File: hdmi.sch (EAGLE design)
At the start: 130 parts, among them U0 6SLX45CSG324, U1 MT41J64M16, U2 TPD12S016RKTR, U3 TPD12S016RKTR, U4 TPD12S016RKTR, U5 MNR18, U6 MNR18

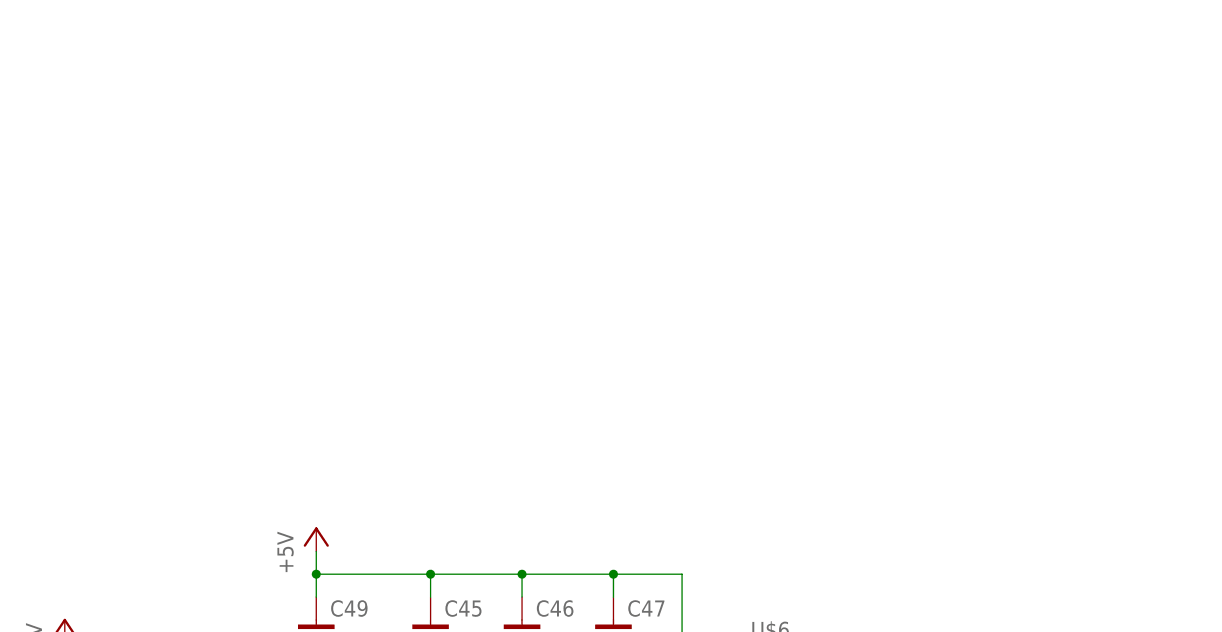
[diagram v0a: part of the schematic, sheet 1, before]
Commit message: +prj-hdmi.lbr, +5V protection
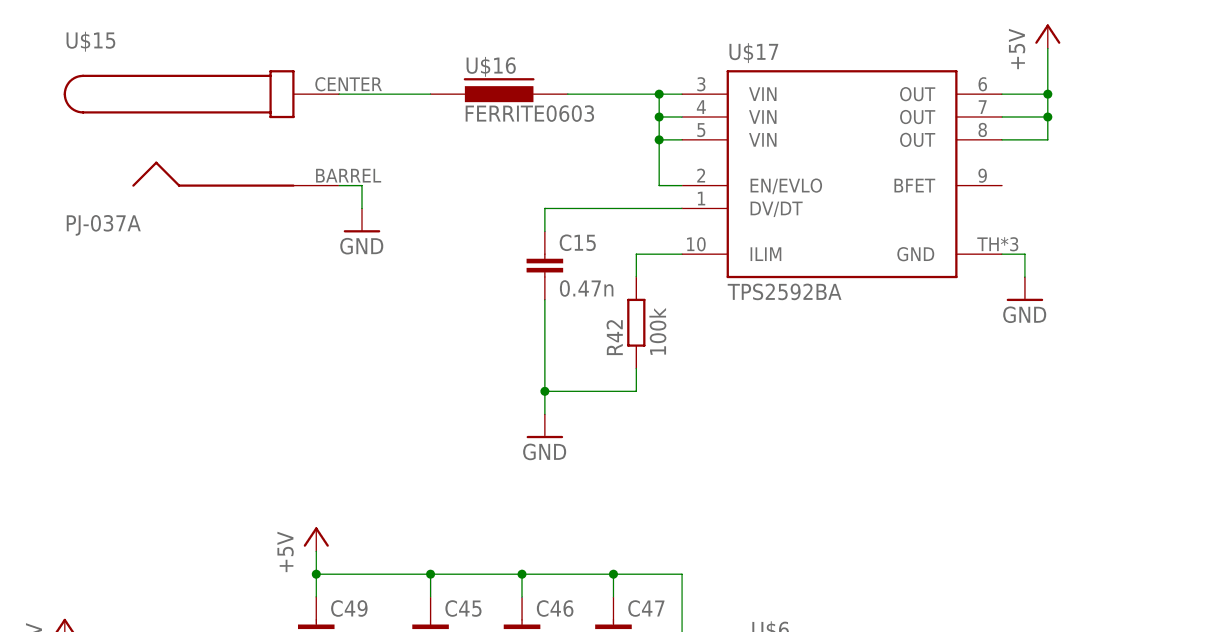
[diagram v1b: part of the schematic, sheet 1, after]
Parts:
- removed R43: 4.7k, resistor:R-EU_R0402
- removed U$12: PJ-037A, con-cui:PJ-037A
- removed U$13: FERRITE0603, inductors:FERRITE0603
- added C15: 0.47n, rcl:C-EUC0402
- added R46: 1k, resistor:R-EU_R0402
- added U$15: PJ-037A, prj-hdmi:PJ-037A
- added U$16: FERRITE0603, inductors:FERRITE0603
- added U$17: TPS2592BA, prj-hdmi:TPS2592BA
- CONN0, CONN1, CONN2: device con-fci:HDMI_TYPE_A_RECEPTICAL -> prj-hdmi:HDMI_TYPE_A_RECEPTICAL
- CONN3: device con-usb-3:USB-MB-S -> prj-hdmi:USB-MB-S
- IC1: device ftdichip-3:FT2232HQ -> prj-hdmi:FT2232HQ
- R42: value 10k -> 100k
- U$1: device Abracon:ABM8G -> prj-hdmi:ABM8G
- U$5: device Microchip_By_element14_Batch_1:93LC46BT-I/OT -> prj-hdmi:93LC46BT-I/OT
- U$6: device Micrel Inc:MIC23451AAAYFL -> prj-hdmi:MIC23451AAAYFL
- U$9: device memory-micron:N25Q128A13EF8 -> prj-hdmi:N25Q128A13EF8
- U0: device xilinx_devices_V6:6SLX45CSG324 -> prj-hdmi:6SLX45CSG324
- U1: device memory-micron:MT41J64M16 -> prj-hdmi:MT41J64M16
- U2, U3, U4: device Texas Instruments:TPD12S016RKTR -> prj-hdmi:TPD12S016RKTR
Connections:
- net N$49 renamed USB_5V_DISABLE
- removed net USB_5V_ERR: R45.1, U$10.ACK#
- new net N$32: C15.1, U$17.DV/DT
- new net N$36: R42.2, U$17.ILIM
- new net USB_5V_ACK#: R45.1, R46.1, U$10.ACK#
- new net USB_5V_OFF: R46.2
- net +3V3: now also R26.1
- net +5V: now also U$17.OUT@6, U$17.OUT@7, U$17.OUT@8; no longer R43.2
- net CENTER: now also U$15.CENTER, U$16.1; no longer U$12.CENTER, U$13.1
- net GND: now also C15.2, U$15.BARREL, U$17.GND; no longer U$12.BARREL
- net N$29: now also U$16.2, U$17.EN/EVLO, U$17.VIN@3, U$17.VIN@4, U$17.VIN@5; no longer R26.1
- net USB_PWRSAVE#: no longer R42.2, R43.1
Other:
- moved on the sheet: R45

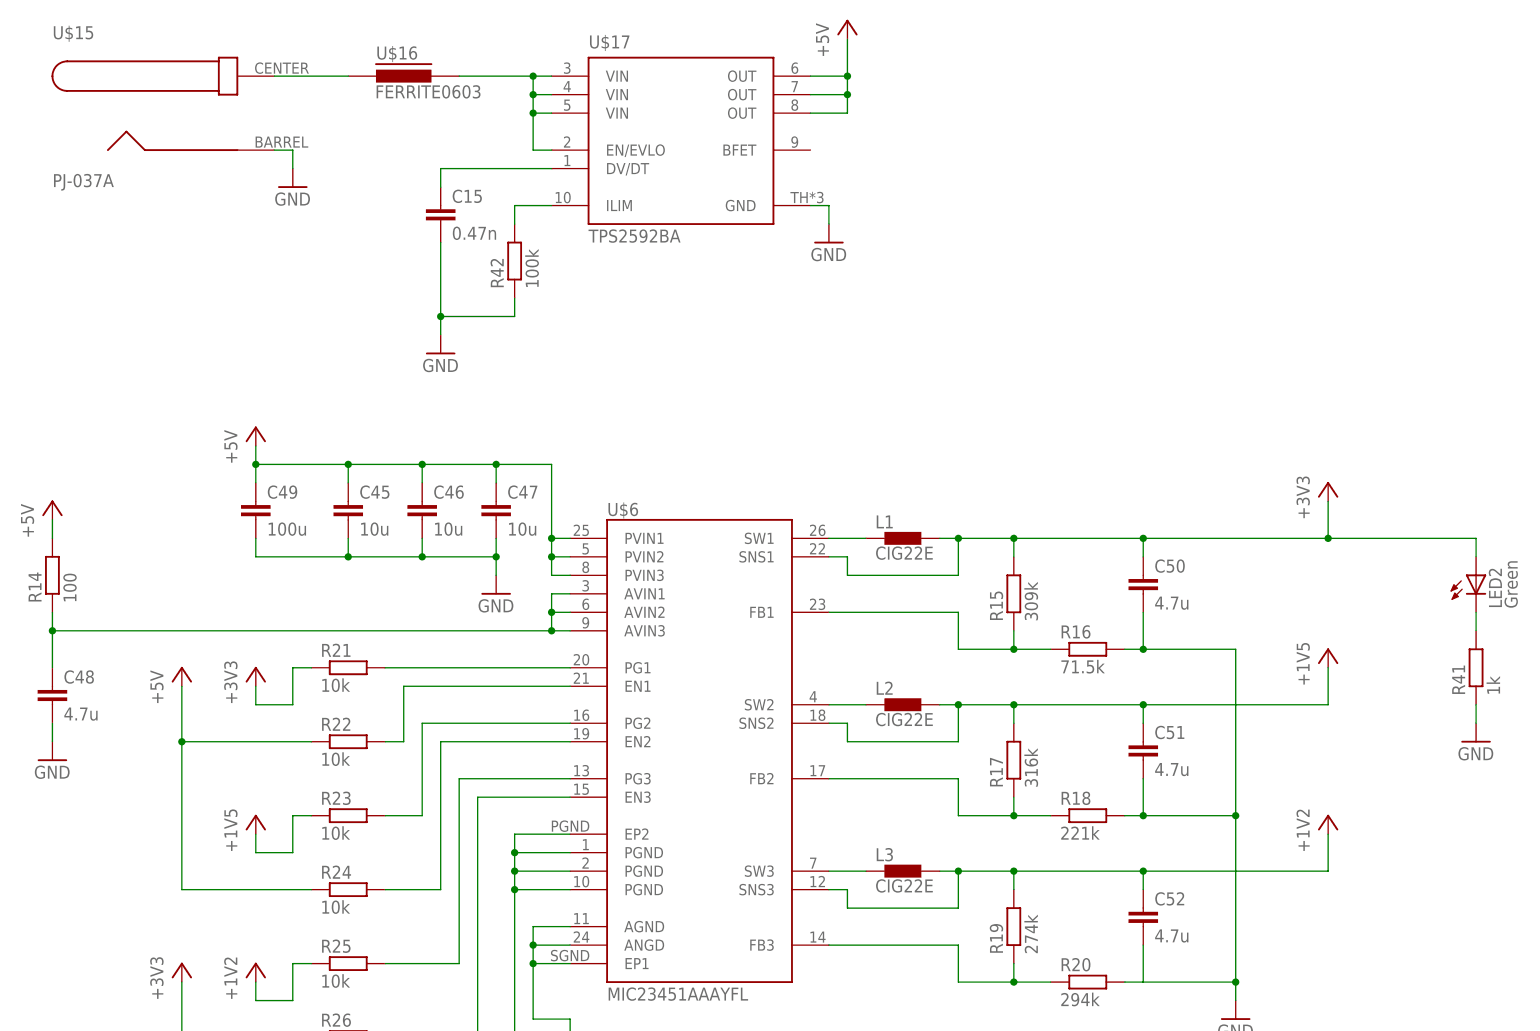
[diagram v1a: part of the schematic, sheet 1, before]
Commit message: began mergin and cleaning up libraries
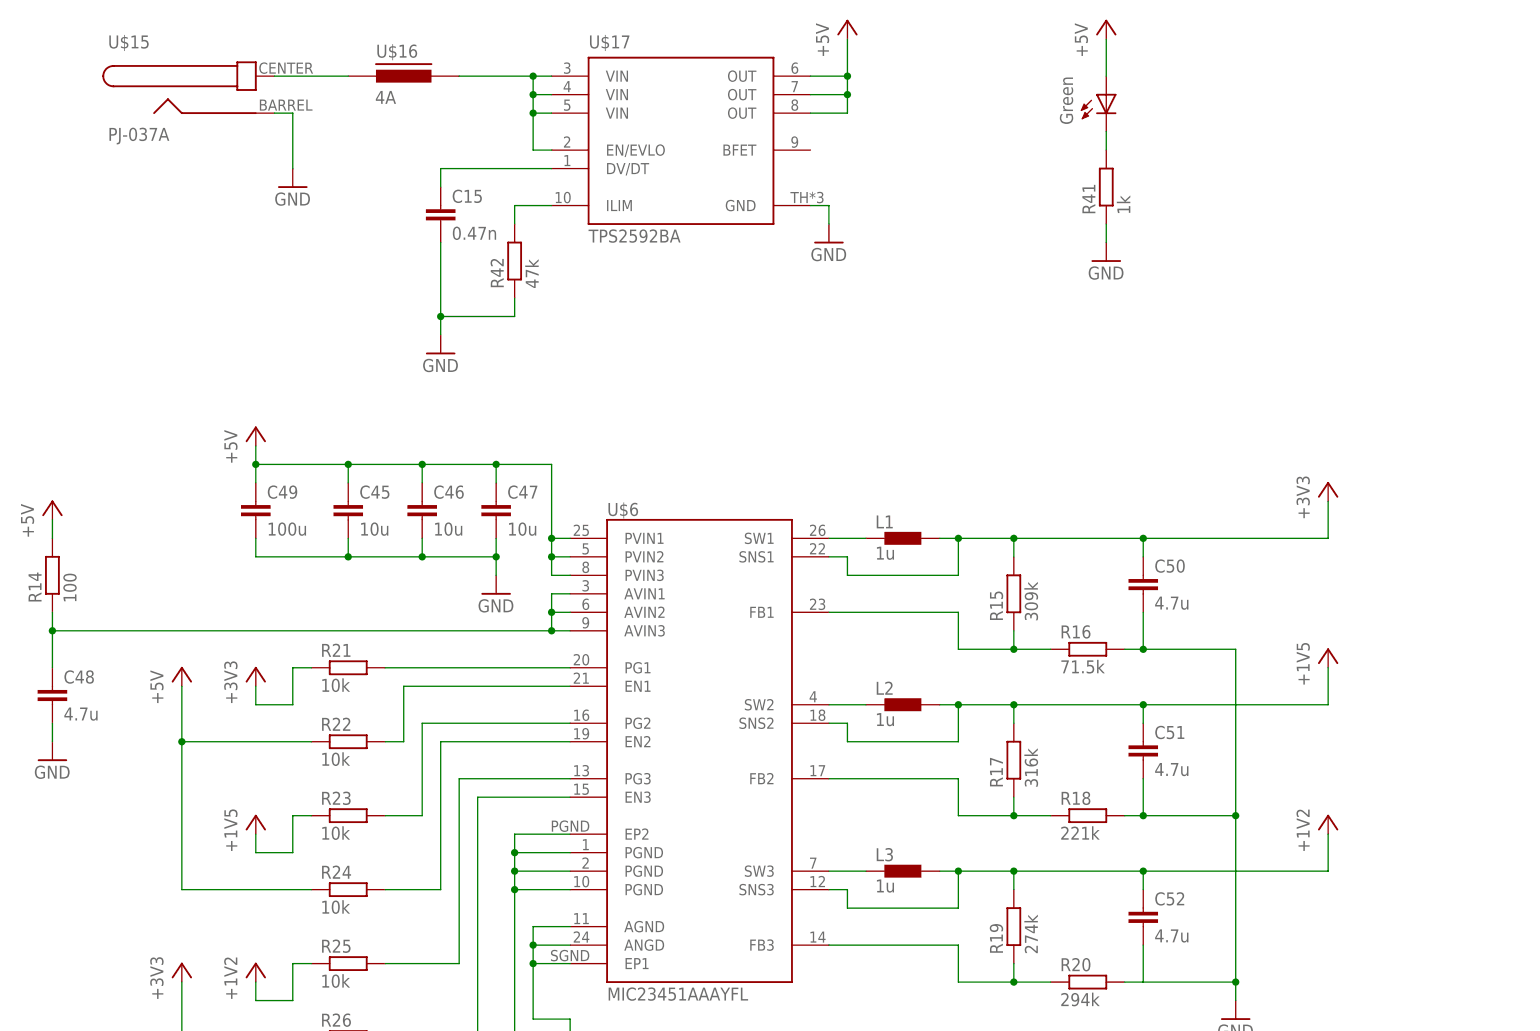
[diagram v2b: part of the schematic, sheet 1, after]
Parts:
- removed C7: 100u, rcl:C-EUC1206
- removed U$11: FERRITE0603, inductors:FERRITE0603
- added L6: 1A, prj-hdmi:FERRITE0603
- added R43: 10k, resistor:R-EU_R0402
- CONN3: device prj-hdmi:USB-MB-S -> prj-hdmi:USBMB-S
- L1, L2, L3: value CIG22E -> 1u; device inductors:CIG22E -> prj-hdmi:INDUCTOR1008
- L4, L5: value FERRITE0402 -> 1A; device inductors:FERRITE0402 -> prj-hdmi:FERRITE0402
- LED1, LED2: device led:LEDCHIP-LED0603 -> prj-hdmi:LED0603
- R42: value 100k -> 47k
- U$10: value TPD4S014DSQRSON -> TPD4S014SON; device Texas Instruments:TPD4S014DSQRSON -> Texas Instruments:TPD4S014SON
- U$16: value FERRITE0603 -> 4A; device inductors:FERRITE0603 -> prj-hdmi:FERRITE0603
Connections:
- net +1V5: no longer C7.1
- net +3V3: now also R43.2; no longer LED2.A
- net GND: no longer C7.2
- net N$45: now also L6.1; no longer U$11.1
- net N$48: now also L6.2; no longer U$11.2
- net USB_PWRSAVE#: now also R43.1
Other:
- moved on the sheet: R41, U$15

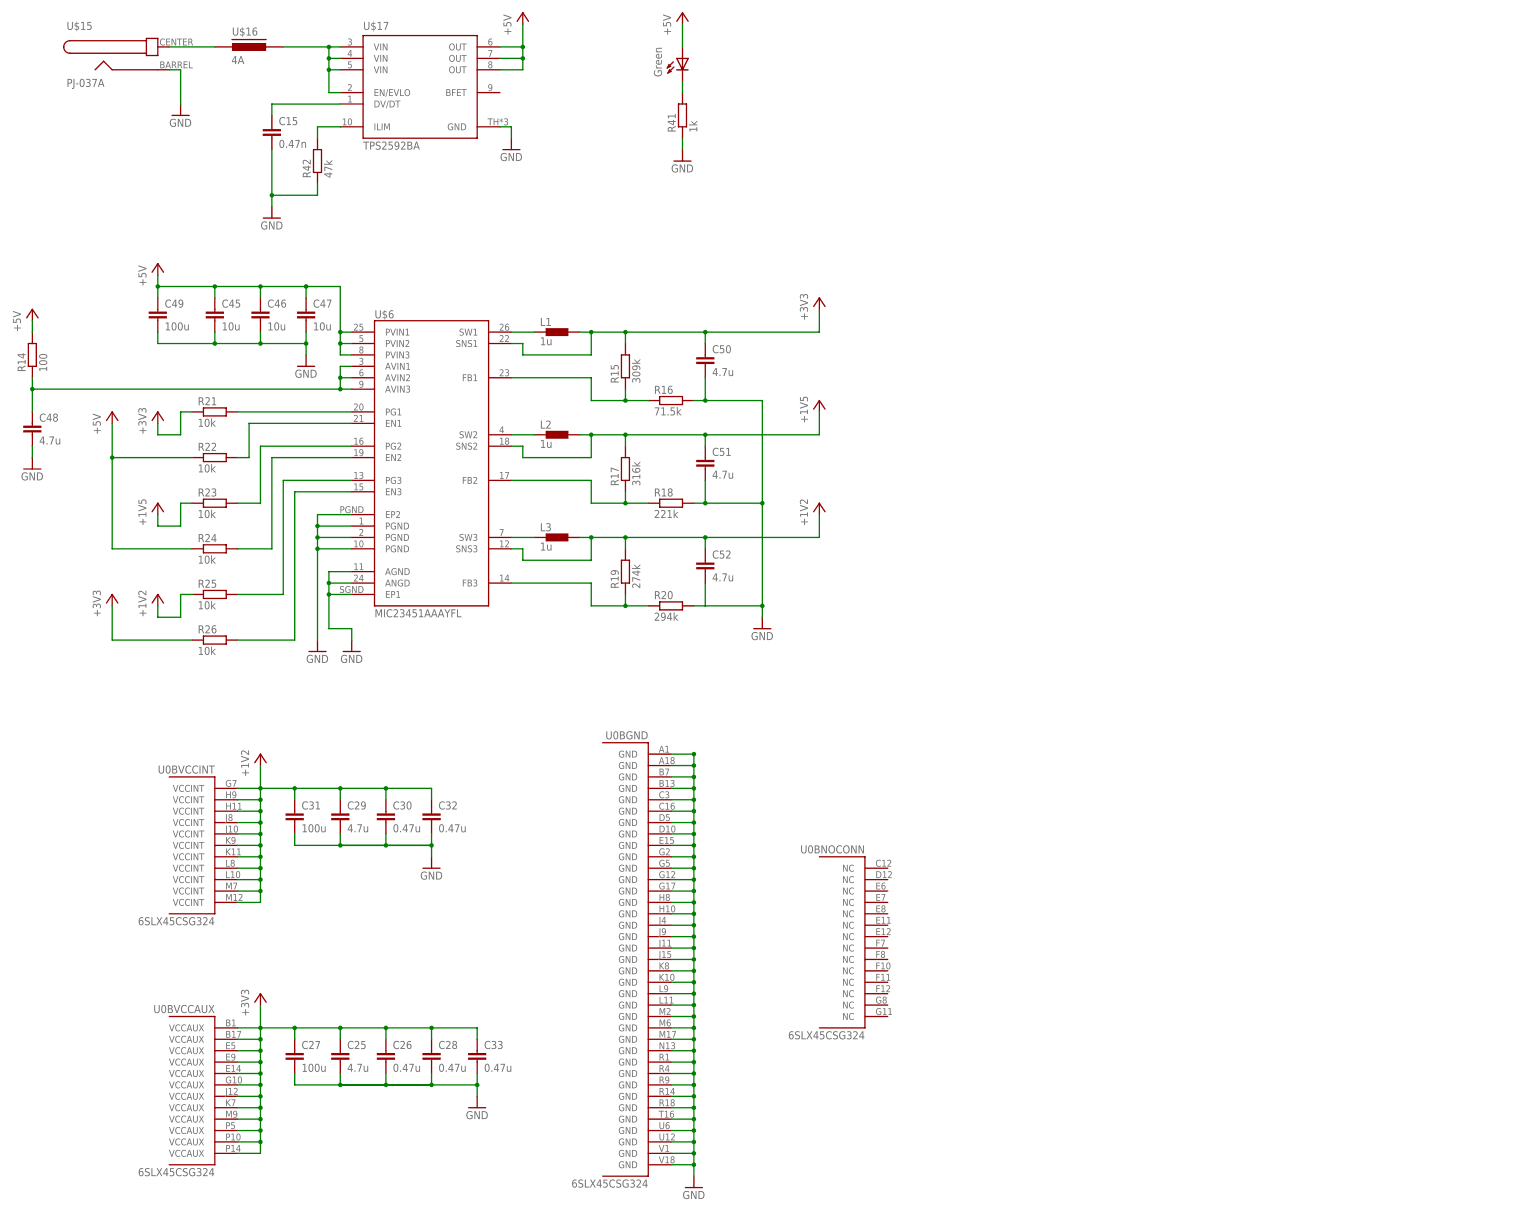
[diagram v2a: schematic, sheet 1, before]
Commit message: +5V supply zener diode and minor misc. changes
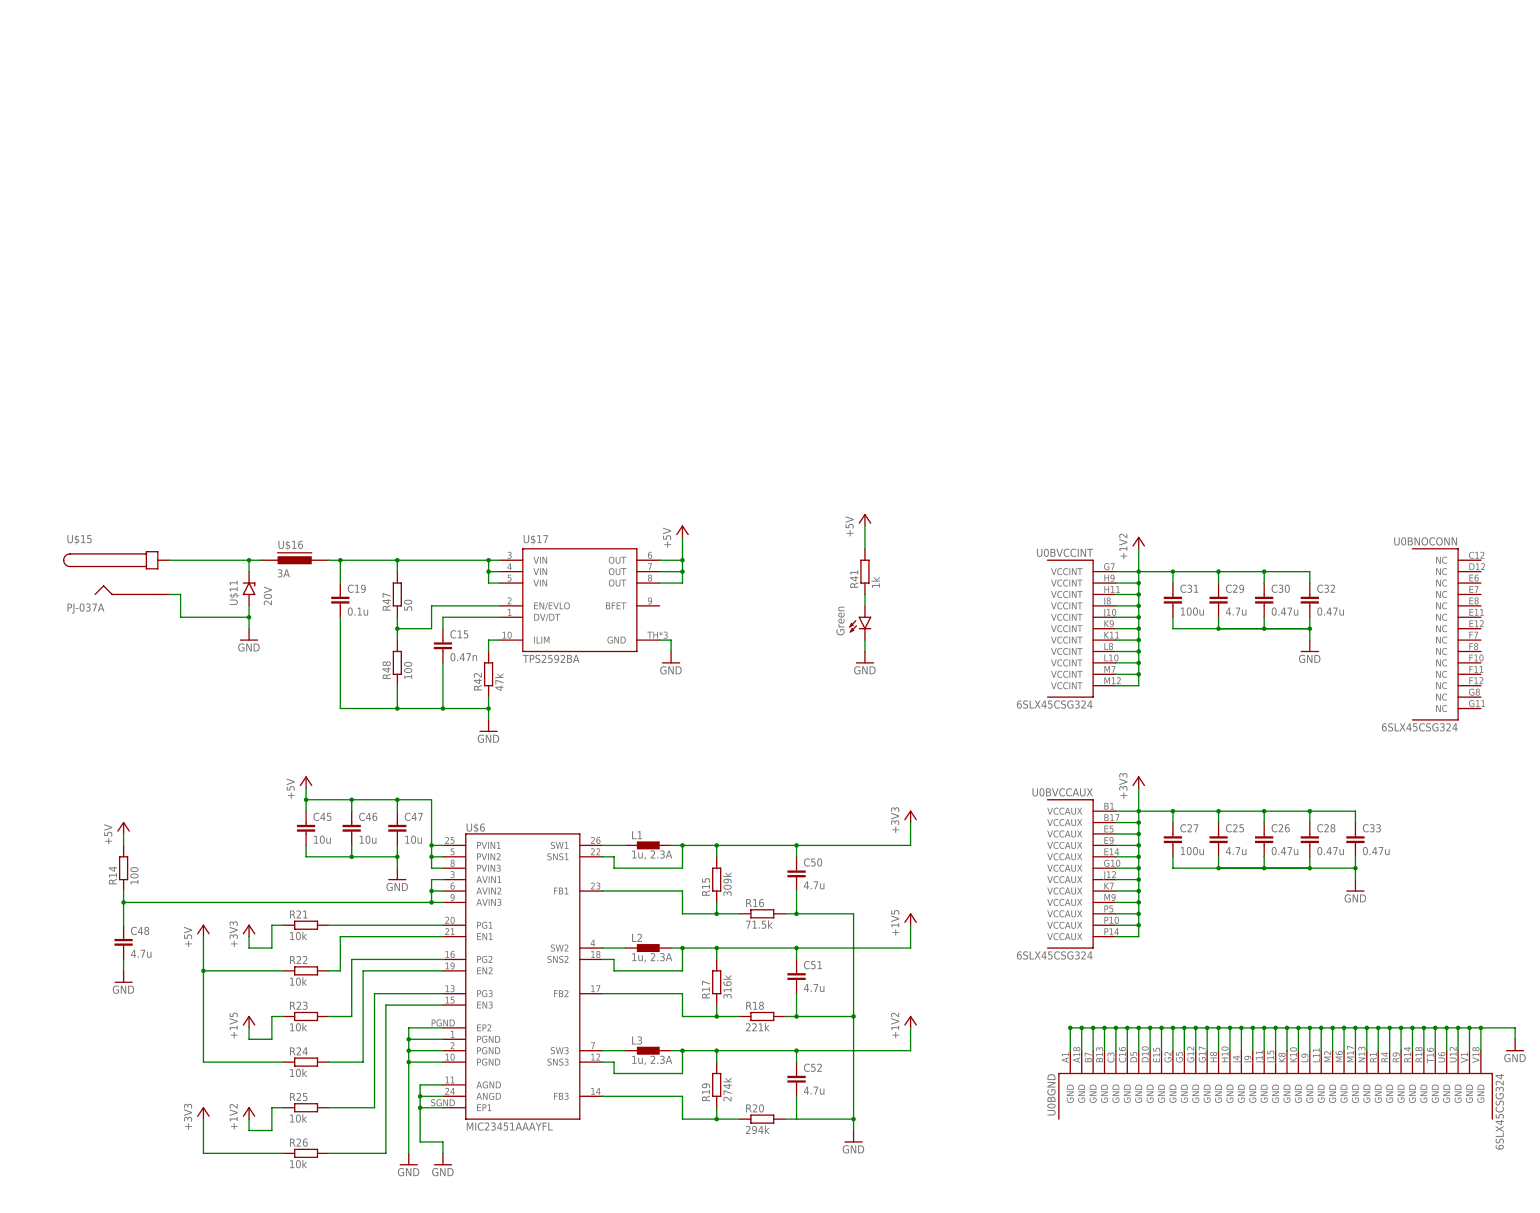
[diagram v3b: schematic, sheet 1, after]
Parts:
- removed C49: 100u, rcl:C-EUC1206
- added C19: 0.1u, prj-hdmi:C-EU0603
- added C7: 100u, prj-hdmi:C-EU0603
- added R47: 50, resistor:R-EU_R0402
- added R48: 100, resistor:R-EU_R0402
- added U$11: 20V, prj-hdmi:ZENER-DIODESOD123FL
- L1, L2, L3: value 1u -> 1u, 2.3A
- U$16: value 4A -> 3A
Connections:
- net +3V3: now also R27.2; no longer LED1.A
- net +5V: now also R41.2; no longer C49.1
- net CENTER: now also U$11.C
- net GND: now also C19.2, C7.2, LED2.C, R48.1, U$11.A, U$6.AGND@11, U$6.ANGD@24, U$6.EP1; no longer C49.2, R41.1
- net N$29: now also C19.1, R47.2; no longer U$17.EN/EVLO
- net N$30: now also R47.1, R48.2, U$17.EN/EVLO; no longer U$6.AGND@11, U$6.ANGD@24, U$6.EP1
- net N$33: now also LED1.C; no longer R27.1
- net N$38: now also LED1.A, R27.1; no longer LED1.C, R27.2
- net N$47: now also LED2.A, R41.1; no longer LED2.C, R41.2
- net N$48: now also C7.1
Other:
- moved on the sheet: C15, C25, C26, C27, C28, C29, C30, C31, C32, C33, C45, C46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
